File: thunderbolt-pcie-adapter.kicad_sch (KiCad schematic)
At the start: 8 parts

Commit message: [#58582] Globlib
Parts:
- FID1, FID2, FID3, FID4, FID5, FID6, FID7, FID8: footprint thunderbolt-pcie-adapter-footprints:Fiducial_1mm_Mask3mm -> antmicro-footprints:Fiducial_1mm_Mask3mm; symbol thunderbolt-pcie-adapter:Fiducial_1mm_Mask3mm -> antmicroFiducialMarks:Fiducial_1mm_Mask3mm
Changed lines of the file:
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@@
     (effects (font (size 2.54 2.54) bold) (justify left bottom))
   )
-  (symbol (lib_id "thunderbolt-pcie-adapter:Fiducial_1mm_Mask3mm") (at 29.21 269.875 0) (unit 1)
+  (symbol (lib_id "antmicroFiducialMarks:Fiducial_1mm_Mask3mm") (at 29.21 269.875 0) (unit 1)
     (in_bom no) (on_board yes) (dnp no) (fields_autoplaced)
     (property "Reference" "FID4" (at 34.29 268.6049 0)
@@
       (effects (font (size 1.27 1.27) (thickness 0.15)) (justify left))
     )
-    (property "Footprint" "thunderbolt-pcie-adapter-footprints:Fiducial_1mm_Mask3mm" (at 46.99 277.495 0)
+    (property "Footprint" "antmicro-footprints:Fiducial_1mm_Mask3mm" (at 46.99 277.495 0)
       (effects (font (size 1.27 1.27) (thickness 0.15)) (justify left bottom) hide)
     )
@@
     )
   )
-  (symbol (lib_id "thunderbolt-pcie-adapter:Fiducial_1mm_Mask3mm") (at 29.21 255.905 0) (unit 1)
+  (symbol (lib_id "antmicroFiducialMarks:Fiducial_1mm_Mask3mm") (at 29.21 255.905 0) (unit 1)
     (in_bom no) (on_board yes) (dnp no) (fields_autoplaced)
     (property "Reference" "FID2" (at 34.29 254.6349 0)
@@
       (effects (font (size 1.27 1.27) (thickness 0.15)) (justify left))
     )
-    (property "Footprint" "thunderbolt-pcie-adapter-footprints:Fiducial_1mm_Mask3mm" (at 46.99 263.525 0)
+    (property "Footprint" "antmicro-footprints:Fiducial_1mm_Mask3mm" (at 46.99 263.525 0)
       (effects (font (size 1.27 1.27) (thickness 0.15)) (justify left bottom) hide)
     )
@@
     )
   )
-  (symbol (lib_id "thunderbolt-pcie-adapter:Fiducial_1mm_Mask3mm") (at 71.12 262.89 0) (unit 1)
+  (symbol (lib_id "antmicroFiducialMarks:Fiducial_1mm_Mask3mm") (at 71.12 262.89 0) (unit 1)
     (in_bom no) (on_board yes) (dnp no) (fields_autoplaced)
     (property "Reference" "FID7" (at 76.2 261.6199 0)
@@
       (effects (font (size 1.27 1.27) (thickness 0.15)) (justify left))
     )
-    (property "Footprint" "thunderbolt-pcie-adapter-footprints:Fiducial_1mm_Mask3mm" (at 88.9 270.51 0)
+    (property "Footprint" "antmicro-footprints:Fiducial_1mm_Mask3mm" (at 88.9 270.51 0)
       (effects (font (size 1.27 1.27) (thickness 0.15)) (justify left bottom) hide)
     )
@@
     )
   )
-  (symbol (lib_id "thunderbolt-pcie-adapter:Fiducial_1mm_Mask3mm") (at 71.12 269.875 0) (unit 1)
+  (symbol (lib_id "antmicroFiducialMarks:Fiducial_1mm_Mask3mm") (at 71.12 269.875 0) (unit 1)
     (in_bom no) (on_board yes) (dnp no) (fields_autoplaced)
     (property "Reference" "FID8" (at 76.2 268.6049 0)
@@
       (effects (font (size 1.27 1.27) (thickness 0.15)) (justify left))
     )
-    (property "Footprint" "thunderbolt-pcie-adapter-footprints:Fiducial_1mm_Mask3mm" (at 88.9 277.495 0)
+    (property "Footprint" "antmicro-footprints:Fiducial_1mm_Mask3mm" (at 88.9 277.495 0)
       (effects (font (size 1.27 1.27) (thickness 0.15)) (justify left bottom) hide)
     )
@@
     )
   )
-  (symbol (lib_id "thunderbolt-pcie-adapter:Fiducial_1mm_Mask3mm") (at 29.21 262.89 0) (unit 1)
+  (symbol (lib_id "antmicroFiducialMarks:Fiducial_1mm_Mask3mm") (at 29.21 262.89 0) (unit 1)
     (in_bom no) (on_board yes) (dnp no) (fields_autoplaced)
     (property "Reference" "FID3" (at 34.29 261.6199 0)
@@
       (effects (font (size 1.27 1.27) (thickness 0.15)) (justify left))
     )
-    (property "Footprint" "thunderbolt-pcie-adapter-footprints:Fiducial_1mm_Mask3mm" (at 46.99 270.51 0)
+    (property "Footprint" "antmicro-footprints:Fiducial_1mm_Mask3mm" (at 46.99 270.51 0)
       (effects (font (size 1.27 1.27) (thickness 0.15)) (justify left bottom) hide)
     )
@@
     )
   )
-  (symbol (lib_id "thunderbolt-pcie-adapter:Fiducial_1mm_Mask3mm") (at 29.21 248.92 0) (unit 1)
+  (symbol (lib_id "antmicroFiducialMarks:Fiducial_1mm_Mask3mm") (at 29.21 248.92 0) (unit 1)
     (in_bom no) (on_board yes) (dnp no) (fields_autoplaced)
     (property "Reference" "FID1" (at 34.29 247.6499 0)
@@
       (effects (font (size 1.27 1.27) (thickness 0.15)) (justify left))
     )
-    (property "Footprint" "thunderbolt-pcie-adapter-footprints:Fiducial_1mm_Mask3mm" (at 46.99 256.54 0)
+    (property "Footprint" "antmicro-footprints:Fiducial_1mm_Mask3mm" (at 46.99 256.54 0)
       (effects (font (size 1.27 1.27) (thickness 0.15)) (justify left bottom) hide)
     )
@@
     )
   )
-  (symbol (lib_id "thunderbolt-pcie-adapter:Fiducial_1mm_Mask3mm") (at 71.12 255.905 0) (unit 1)
+  (symbol (lib_id "antmicroFiducialMarks:Fiducial_1mm_Mask3mm") (at 71.12 255.905 0) (unit 1)
     (in_bom no) (on_board yes) (dnp no) (fields_autoplaced)
     (property "Reference" "FID6" (at 76.2 254.6349 0)
@@
       (effects (font (size 1.27 1.27) (thickness 0.15)) (justify left))
     )
-    (property "Footprint" "thunderbolt-pcie-adapter-footprints:Fiducial_1mm_Mask3mm" (at 88.9 263.525 0)
+    (property "Footprint" "antmicro-footprints:Fiducial_1mm_Mask3mm" (at 88.9 263.525 0)
       (effects (font (size 1.27 1.27) (thickness 0.15)) (justify left bottom) hide)
     )
@@
     )
   )
-  (symbol (lib_id "thunderbolt-pcie-adapter:Fiducial_1mm_Mask3mm") (at 71.12 248.92 0) (unit 1)
+  (symbol (lib_id "antmicroFiducialMarks:Fiducial_1mm_Mask3mm") (at 71.12 248.92 0) (unit 1)
     (in_bom no) (on_board yes) (dnp no) (fields_autoplaced)
     (property "Reference" "FID5" (at 76.2 247.6499 0)
@@
       (effects (font (size 1.27 1.27) (thickness 0.15)) (justify left))
     )
-    (property "Footprint" "thunderbolt-pcie-adapter-footprints:Fiducial_1mm_Mask3mm" (at 88.9 256.54 0)
-      (effects (font (size 1.27 1.27) (thickness 0.15)) (justify left bottom) hide)
-    )
+    (property "Footprint" "antmicro-footprints:Fiducial_1mm_Mask3mm" (at 88.9 256.54 0)
+      (effects (font (size 1.27 1.27) (thickness 0.15)) (justify left bottom) hide)
+    )

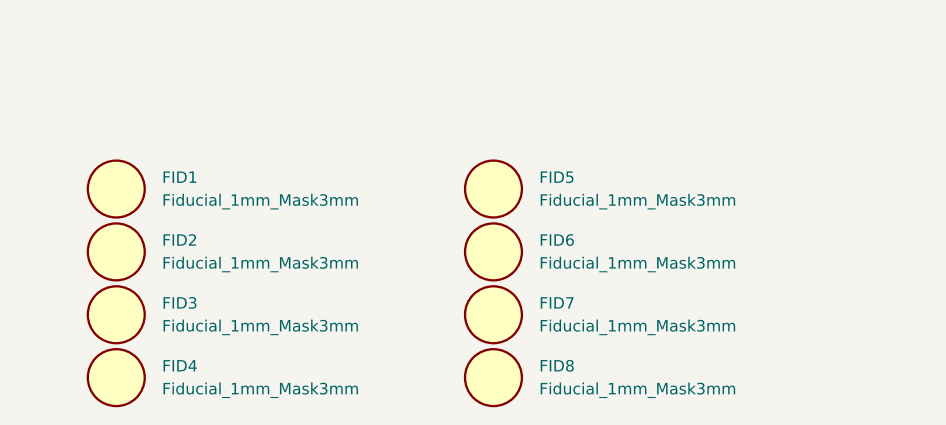
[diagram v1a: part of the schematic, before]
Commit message: [#58582] WiP: Update symbols to global
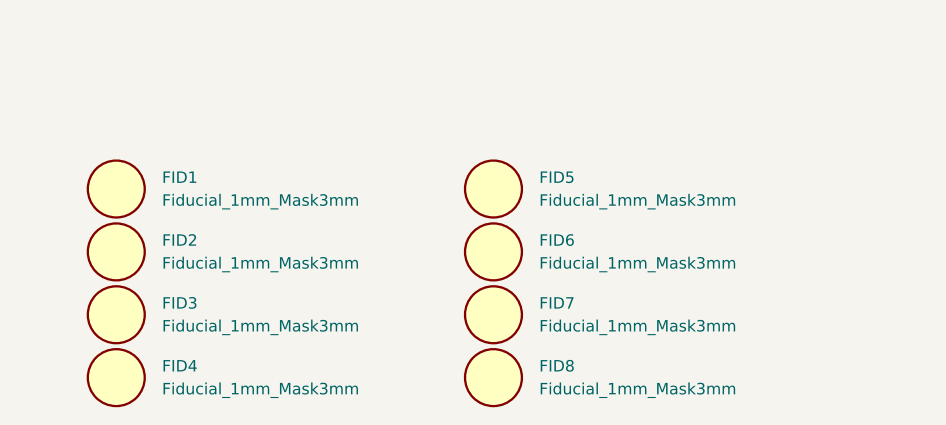
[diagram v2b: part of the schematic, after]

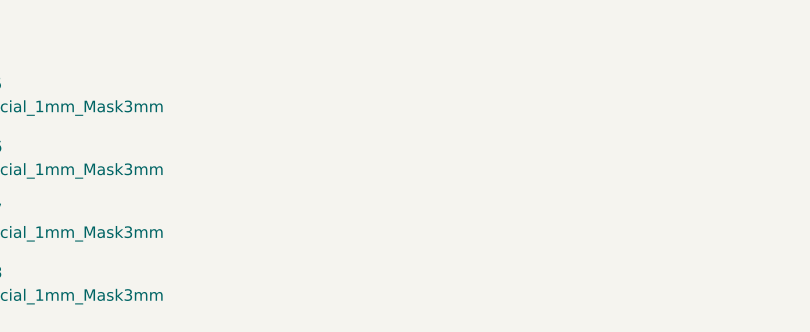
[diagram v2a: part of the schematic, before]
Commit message: [#58582] Update symbols values visibility
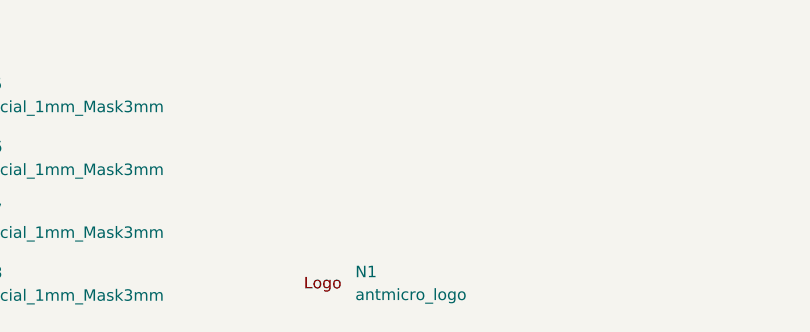
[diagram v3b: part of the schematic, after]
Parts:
- added N1: antmicro_logo, antmicro-footprints:antmicro-logo_scaled_12mm_mask, symbol antmicroMechanicalParts:antmicro_logo
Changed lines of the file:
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@@
+    )
+  )
+  (symbol (lib_id "antmicroMechanicalParts:antmicro_logo") (at 113.665 270.51 0) (unit 1)
+    (in_bom no) (on_board yes) (dnp no) (fields_autoplaced)
+    (property "Reference" "N1" (at 119.38 268.5262 0)
+      (effects (font (size 1.27 1.27) (thickness 0.15)) (justify left))
+    )
+    (property "Value" "antmicro_logo" (at 119.38 271.0662 0)
+      (effects (font (size 1.27 1.27) (thickness 0.15)) (justify left))
+    )
+    (property "Footprint" "antmicro-footprints:antmicro-logo_scaled_12mm_mask" (at 128.905 280.67 0)
+      (effects (font (size 1.27 1.27) (thickness 0.15)) (justify left bottom) hide)
+    )
+    (property "Datasheet" "" (at 128.905 283.21 0)
+      (effects (font (size 1.27 1.27) (thickness 0.15)) (justify left bottom) hide)
+    )
+    (property "MPN" "" (at 113.665 270.51 0)
+      (effects (font (size 1.27 1.27)))
+    )
+    (property "Manufacturer" "" (at 128.905 290.83 0)
+      (effects (font (size 1.27 1.27) (thickness 0.15)) (justify left bottom) hide)
+    )
+    (property "Author" "Antmicro" (at 128.905 285.75 0)
+      (effects (font (size 1.27 1.27) (thickness 0.15)) (justify left bottom) hide)
+    )
+    (property "License" "Apache-2.0" (at 128.905 288.29 0)
+      (effects (font (size 1.27 1.27) (thickness 0.15)) (justify left bottom) hide)
+    )
+    (instances
+      (project "thunderbolt-pcie-adapter"
+        (path "/6701ed44-03d2-4633-acc7-b19b85d75ead"
+          (reference "N1") (unit 1)
+        )
+      )
     )
   )

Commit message: [#61922] Update all symbols, clean ERC
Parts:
- FID1, FID2, FID3, FID4, FID5, FID6, FID7, FID8: Public (none) -> False
- N1: footprint antmicro-footprints:antmicro-logo_scaled_12mm_mask -> antmicro-footprints:antmicro-logo; Public (none) -> False
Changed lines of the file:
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@@
       (effects (font (size 1.27 1.27) (thickness 0.15)) (justify left bottom) hide)
+    )
+    (property "Public" "False" (at 36.83 282.575 0)
+      (effects (font (size 1.27 1.27)) (justify left bottom) hide)
     )
     (instances
@@
     )
   )
-  (symbol (lib_name "Fiducial_1mm_Mask3mm_7") (lib_id "antmicroFiducialMarks:Fiducial_1mm_Mask3mm") (at 29.21 255.905 0) (unit 1)
+  (symbol (lib_id "antmicroFiducialMarks:Fiducial_1mm_Mask3mm") (at 29.21 255.905 0) (unit 1)
     (in_bom no) (on_board yes) (dnp no) (fields_autoplaced)
     (property "Reference" "FID2" (at 34.29 254.635 0)
@@
       (effects (font (size 1.27 1.27) (thickness 0.15)) (justify left bottom) hide)
     )
+    (property "Public" "False" (at 36.83 268.605 0)
+      (effects (font (size 1.27 1.27)) (justify left bottom) hide)
+    )
     (instances
       (project "thunderbolt-pcie-adapter"
@@
       (effects (font (size 1.27 1.27) (thickness 0.15)) (justify left))
     )
-    (property "Footprint" "antmicro-footprints:antmicro-logo_scaled_12mm_mask" (at 128.905 280.67 0)
+    (property "Footprint" "antmicro-footprints:antmicro-logo" (at 128.905 280.67 0)
       (effects (font (size 1.27 1.27) (thickness 0.15)) (justify left bottom) hide)
     )
@@
       (effects (font (size 1.27 1.27) (thickness 0.15)) (justify left bottom) hide)
     )
+    (property "Public" "False" (at 128.905 290.83 0)
+      (effects (font (size 1.27 1.27)) (justify left bottom) hide)
+    )
     (instances
       (project "thunderbolt-pcie-adapter"
@@
     )
   )
-  (symbol (lib_name "Fiducial_1mm_Mask3mm_6") (lib_id "antmicroFiducialMarks:Fiducial_1mm_Mask3mm") (at 71.12 262.89 0) (unit 1)
+  (symbol (lib_id "antmicroFiducialMarks:Fiducial_1mm_Mask3mm") (at 71.12 262.89 0) (unit 1)
     (in_bom no) (on_board yes) (dnp no) (fields_autoplaced)
     (property "Reference" "FID7" (at 76.2 261.62 0)
@@
       (effects (font (size 1.27 1.27) (thickness 0.15)) (justify left bottom) hide)
     )
+    (property "Public" "False" (at 78.74 275.59 0)
+      (effects (font (size 1.27 1.27)) (justify left bottom) hide)
+    )
     (instances
       (project "thunderbolt-pcie-adapter"
@@
     )
   )
-  (symbol (lib_name "Fiducial_1mm_Mask3mm_5") (lib_id "antmicroFiducialMarks:Fiducial_1mm_Mask3mm") (at 71.12 269.875 0) (unit 1)
+  (symbol (lib_id "antmicroFiducialMarks:Fiducial_1mm_Mask3mm") (at 71.12 269.875 0) (unit 1)
     (in_bom no) (on_board yes) (dnp no) (fields_autoplaced)
     (property "Reference" "FID8" (at 76.2 268.605 0)
@@
       (effects (font (size 1.27 1.27) (thickness 0.15)) (justify left bottom) hide)
     )
+    (property "Public" "False" (at 78.74 282.575 0)
+      (effects (font (size 1.27 1.27)) (justify left bottom) hide)
+    )
     (instances
       (project "thunderbolt-pcie-adapter"
@@
     )
   )
-  (symbol (lib_name "Fiducial_1mm_Mask3mm_4") (lib_id "antmicroFiducialMarks:Fiducial_1mm_Mask3mm") (at 29.21 262.89 0) (unit 1)
+  (symbol (lib_id "antmicroFiducialMarks:Fiducial_1mm_Mask3mm") (at 29.21 262.89 0) (unit 1)
     (in_bom no) (on_board yes) (dnp no) (fields_autoplaced)
     (property "Reference" "FID3" (at 34.29 261.62 0)
@@
       (effects (font (size 1.27 1.27) (thickness 0.15)) (justify left bottom) hide)
     )
+    (property "Public" "False" (at 36.83 275.59 0)
+      (effects (font (size 1.27 1.27)) (justify left bottom) hide)
+    )
     (instances
       (project "thunderbolt-pcie-adapter"
@@
     )
   )
-  (symbol (lib_name "Fiducial_1mm_Mask3mm_3") (lib_id "antmicroFiducialMarks:Fiducial_1mm_Mask3mm") (at 29.21 248.92 0) (unit 1)
+  (symbol (lib_id "antmicroFiducialMarks:Fiducial_1mm_Mask3mm") (at 29.21 248.92 0) (unit 1)
     (in_bom no) (on_board yes) (dnp no) (fields_autoplaced)
     (property "Reference" "FID1" (at 34.29 247.65 0)
@@
       (effects (font (size 1.27 1.27) (thickness 0.15)) (justify left bottom) hide)
     )
+    (property "Public" "False" (at 36.83 261.62 0)
+      (effects (font (size 1.27 1.27)) (justify left bottom) hide)
+    )
     (instances
       (project "thunderbolt-pcie-adapter"
@@
     )
   )
-  (symbol (lib_name "Fiducial_1mm_Mask3mm_2") (lib_id "antmicroFiducialMarks:Fiducial_1mm_Mask3mm") (at 71.12 255.905 0) (unit 1)
+  (symbol (lib_id "antmicroFiducialMarks:Fiducial_1mm_Mask3mm") (at 71.12 255.905 0) (unit 1)
     (in_bom no) (on_board yes) (dnp no) (fields_autoplaced)
     (property "Reference" "FID6" (at 76.2 254.635 0)
@@
       (effects (font (size 1.27 1.27) (thickness 0.15)) (justify left bottom) hide)
     )
+    (property "Public" "False" (at 78.74 268.605 0)
+      (effects (font (size 1.27 1.27)) (justify left bottom) hide)
+    )
     (instances
       (project "thunderbolt-pcie-adapter"
@@
     )
   )
-  (symbol (lib_name "Fiducial_1mm_Mask3mm_1") (lib_id "antmicroFiducialMarks:Fiducial_1mm_Mask3mm") (at 71.12 248.92 0) (unit 1)
+  (symbol (lib_id "antmicroFiducialMarks:Fiducial_1mm_Mask3mm") (at 71.12 248.92 0) (unit 1)
     (in_bom no) (on_board yes) (dnp no) (fields_autoplaced)
     (property "Reference" "FID5" (at 76.2 247.65 0)
@@
       (effects (font (size 1.27 1.27) (thickness 0.15)) (justify left bottom) hide)
     )
-    (instances
+    (property "Public" "False" (at 78.74 261.62 0)
+      (effects (font (size 1.27 1.27)) (justify left bottom) hide)
+    )
+    (instances

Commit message: [#61922] Update all footprints, clean DRC errors
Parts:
- N1: footprint antmicro-footprints:antmicro-logo -> antmicro-footprints:antmicro-logo_scaled_12mm_mask
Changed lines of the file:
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@@
       (effects (font (size 1.27 1.27) (thickness 0.15)) (justify left))
     )
-    (property "Footprint" "antmicro-footprints:antmicro-logo" (at 128.905 280.67 0)
+    (property "Footprint" "antmicro-footprints:antmicro-logo_scaled_12mm_mask" (at 128.905 280.67 0)
       (effects (font (size 1.27 1.27) (thickness 0.15)) (justify left bottom) hide)
     )

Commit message: [#61922] Perform kmake dnp & update symbols
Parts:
- FID1, FID2, FID3, FID4, FID5, FID6, FID7, FID8: Public False -> (none)
- N1: footprint antmicro-footprints:antmicro-logo_scaled_12mm_mask -> antmicro-footprints:antmicro-logo; Public False -> (none)
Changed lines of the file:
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@@
       (effects (font (size 1.27 1.27) (thickness 0.15)) (justify left bottom) hide)
-    )
-    (property "Public" "False" (at 36.83 282.575 0)
-      (effects (font (size 1.27 1.27)) (justify left bottom) hide)
     )
     (instances
@@
       (effects (font (size 1.27 1.27) (thickness 0.15)) (justify left bottom) hide)
     )
-    (property "Public" "False" (at 36.83 268.605 0)
-      (effects (font (size 1.27 1.27)) (justify left bottom) hide)
-    )
     (instances
       (project "thunderbolt-pcie-adapter"
@@
       (effects (font (size 1.27 1.27) (thickness 0.15)) (justify left))
     )
-    (property "Footprint" "antmicro-footprints:antmicro-logo_scaled_12mm_mask" (at 128.905 280.67 0)
+    (property "Footprint" "antmicro-footprints:antmicro-logo" (at 128.905 280.67 0)
       (effects (font (size 1.27 1.27) (thickness 0.15)) (justify left bottom) hide)
     )
@@
       (effects (font (size 1.27 1.27) (thickness 0.15)) (justify left bottom) hide)
     )
-    (property "Public" "False" (at 128.905 290.83 0)
-      (effects (font (size 1.27 1.27)) (justify left bottom) hide)
-    )
     (instances
       (project "thunderbolt-pcie-adapter"
@@
       (effects (font (size 1.27 1.27) (thickness 0.15)) (justify left bottom) hide)
     )
-    (property "Public" "False" (at 78.74 275.59 0)
-      (effects (font (size 1.27 1.27)) (justify left bottom) hide)
-    )
     (instances
       (project "thunderbolt-pcie-adapter"
@@
       (effects (font (size 1.27 1.27) (thickness 0.15)) (justify left bottom) hide)
     )
-    (property "Public" "False" (at 78.74 282.575 0)
-      (effects (font (size 1.27 1.27)) (justify left bottom) hide)
-    )
     (instances
       (project "thunderbolt-pcie-adapter"
@@
       (effects (font (size 1.27 1.27) (thickness 0.15)) (justify left bottom) hide)
     )
-    (property "Public" "False" (at 36.83 275.59 0)
-      (effects (font (size 1.27 1.27)) (justify left bottom) hide)
-    )
     (instances
       (project "thunderbolt-pcie-adapter"
@@
       (effects (font (size 1.27 1.27) (thickness 0.15)) (justify left bottom) hide)
     )
-    (property "Public" "False" (at 36.83 261.62 0)
-      (effects (font (size 1.27 1.27)) (justify left bottom) hide)
-    )
     (instances
       (project "thunderbolt-pcie-adapter"
@@
       (effects (font (size 1.27 1.27) (thickness 0.15)) (justify left bottom) hide)
     )
-    (property "Public" "False" (at 78.74 268.605 0)
-      (effects (font (size 1.27 1.27)) (justify left bottom) hide)
-    )
     (instances
       (project "thunderbolt-pcie-adapter"
@@
       (effects (font (size 1.27 1.27) (thickness 0.15)) (justify left bottom) hide)
     )
-    (property "Public" "False" (at 78.74 261.62 0)
-      (effects (font (size 1.27 1.27)) (justify left bottom) hide)
-    )
-    (instances
+    (instances

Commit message: [#61922] Bump revision
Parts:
- N1: footprint antmicro-footprints:antmicro-logo -> antmicro-footprints:antmicro-logo_scaled_12mm_mask
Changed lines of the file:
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@@
   (title_block
     (title "Thunderbolt PCIe Adaper")
-    (date "2023-08-09")
-    (rev "1.0.2")
+    (date "2024-07-09")
+    (rev "1.0.3")
     (comment 1 "www.antmicro.com")
     (comment 2 "Antmicro Ltd.")
@@
       (effects (font (size 1.27 1.27) (thickness 0.15)) (justify left))
     )
-    (property "Footprint" "antmicro-footprints:antmicro-logo" (at 128.905 280.67 0)
+    (property "Footprint" "antmicro-footprints:antmicro-logo_scaled_12mm_mask" (at 128.905 280.67 0)
       (effects (font (size 1.27 1.27) (thickness 0.15)) (justify left bottom) hide)
     )
